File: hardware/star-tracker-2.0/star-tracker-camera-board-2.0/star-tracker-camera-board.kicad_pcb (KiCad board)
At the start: 4 copper layers, 31.5 x 13.6 mm, 43 parts, among them J1 3-1734742-6, U1 AR0134CSSM00SPCA0, U2 TPS70618DRVR, U3 TPS71928-28DRVT, U4 TPS71928-28DRVT, X1 MC2520Z27.0000C19XSH

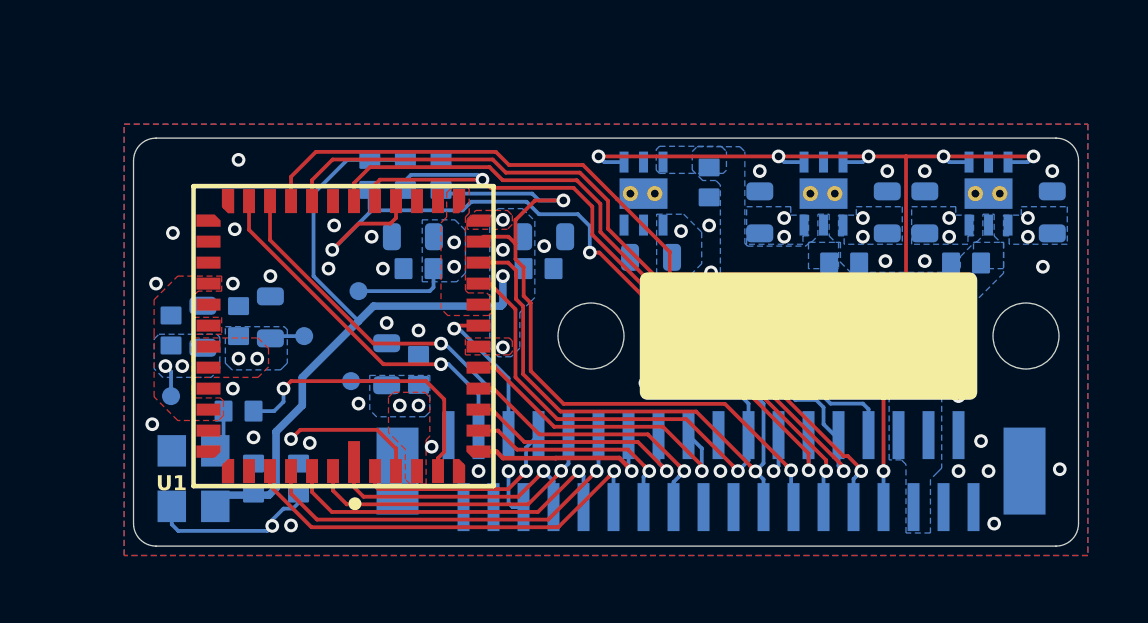
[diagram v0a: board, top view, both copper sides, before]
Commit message: Star tracker camera board
Fixing connector pin out so it fits on board well. Rotated sensor by 90 degrees. Started preliminary board layout
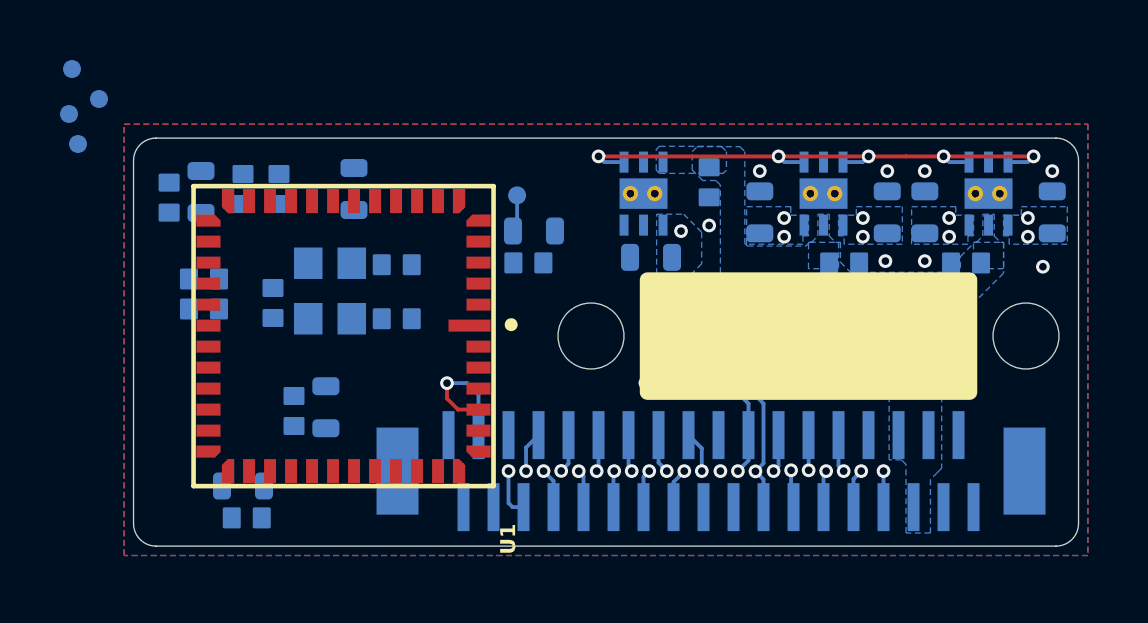
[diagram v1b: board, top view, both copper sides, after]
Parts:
- moved TP8 23.2 mm to (130.7, 95.9)
- moved TP6 11.3 mm to (130.6, 97.4)
- moved TP10 10.5 mm to (131.6, 96.9)
- moved C5 10.2 mm to (136.4, 99.9), turned to 90 degrees
- moved TP9 8.96 mm to (130.9, 98.4)
- moved C3 8.64 mm to (133.9, 100.2), turned to 90 degrees
- moved TP7 8.31 mm to (145.5, 100.1), turned to 90 degrees
- moved R11 8.07 mm to (135.1, 103.9), turned to 0 degrees
- moved X1 7.73 mm to (139.3, 103.3)
- moved C2 7.22 mm to (135.0, 100.0), turned to 90 degrees
- moved R2 7.18 mm to (141.5, 102.4)
- moved C1 7.15 mm to (141.5, 104.2), turned to 180 degrees
- moved C13 6.74 mm to (136.5, 110.9), turned to 180 degrees
- moved C8 6.62 mm to (146.1, 101.3), turned to 0 degrees
- moved C4 6.54 mm to (140.1, 99.9), turned to 90 degrees
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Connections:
- J1 pad 20: /D11 -> unconnected-(J1-Pad20)
- J1 pad 21: /D10 -> unconnected-(J1-Pad21)
- J1 pad 22: /D9 -> unconnected-(J1-Pad22)
- J1 pad 23: /D8 -> unconnected-(J1-Pad23)
- J1 pad 24: /D7 -> unconnected-(J1-Pad24)
- J1 pad 25: /D0 -> unconnected-(J1-Pad25)
- J1 pad 26: /D1 -> unconnected-(J1-Pad26)
- J1 pad 27: /D2 -> unconnected-(J1-Pad27)
- J1 pad 28: /D3 -> unconnected-(J1-Pad28)
- J1 pad 29: /D4 -> unconnected-(J1-Pad29)
- J1 pad 30: /D5 -> unconnected-(J1-Pad30)
- J1 pad 31: /D6 -> unconnected-(J1-Pad31)
- J1 pad 32: /PIXCLK -> unconnected-(J1-Pad32)
- J1 pad 33: /VSYNC -> unconnected-(J1-Pad33)
- J1 pad 34: /HSYNC -> /D0
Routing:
- net VDD_IO: track 40.4 -> 14.1 mm, vias 7 -> 2
- net /STANDBY: track 26.8 -> 1.17 mm, vias 3 -> 1
- net /SADDR: track 27.9 -> 2.41 mm
- net /TRIGGER: track 25.4 -> 0.00 mm, vias 1 -> 0
- net /FLASH: track 25.5 -> 1.36 mm
- net /~{OE}: track 24.7 -> 1.24 mm, vias 2 -> 1
- net /~{RESET}: track 24.0 -> 1.26 mm, vias 2 -> 1
- net /SDATA: track 20.5 -> 4.38 mm
- net /SCLK: track 18.4 -> 2.74 mm
- net /D6: track 14.8 -> 0.00 mm, vias 2 -> 0
- net /VSYNC: track 14.7 -> 0.00 mm, vias 1 -> 0
- net /VREG_EN: track 35.4 -> 22.1 mm, vias 7 -> 6
- net /D1: track 13.2 -> 0.00 mm, vias 1 -> 0
- net /HSYNC: track 12.2 -> 0.00 mm, vias 1 -> 0
- net /D2: track 11.7 -> 0.00 mm, vias 1 -> 0
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- removed copper zone on F.Cu, net VAA
- removed copper zone on F.Cu, net VAA_PIX
- removed copper zone on F.Cu, net VDD
- removed copper zone on F.Cu, net VDD_IO
- removed copper zone on F.Cu, net VDD_PLL

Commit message: Cleaned up files
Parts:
- moved TP8 23.2 mm to (152.6, 103.7)
- moved TP6 11.3 mm to (140.3, 103.3)
- moved TP10 10.5 mm to (138.4, 104.8)
- moved C5 10.2 mm to (146.3, 102.6), turned to 0 degrees
- moved TP9 8.96 mm to (134.0, 106.8)
- moved C3 8.64 mm to (142.3, 102.6), turned to 180 degrees
- moved TP7 8.31 mm to (140.0, 106.3), turned to 180 degrees
- moved R11 8.07 mm to (141.8, 99.4), turned to 90 degrees
- moved X1 7.73 mm to (134.8, 109.6)
- moved C2 7.22 mm to (142.1, 101.5), turned to 180 degrees
- moved R2 7.18 mm to (136.3, 107.3)
- moved C1 7.15 mm to (136.8, 109.6), turned to -90 degrees
- moved C13 6.74 mm to (134.0, 104.6), turned to 90 degrees
- moved C8 6.62 mm to (141.2, 105.7), turned to 90 degrees
- moved C4 6.54 mm to (146.4, 101.5), turned to 0 degrees
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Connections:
- J1 pad 20: unconnected-(J1-Pad20) -> /D11
- J1 pad 21: unconnected-(J1-Pad21) -> /D10
- J1 pad 22: unconnected-(J1-Pad22) -> /D9
- J1 pad 23: unconnected-(J1-Pad23) -> /D8
- J1 pad 24: unconnected-(J1-Pad24) -> /D7
- J1 pad 25: unconnected-(J1-Pad25) -> /D0
- J1 pad 26: unconnected-(J1-Pad26) -> /D1
- J1 pad 27: unconnected-(J1-Pad27) -> /D2
- J1 pad 28: unconnected-(J1-Pad28) -> /D3
- J1 pad 29: unconnected-(J1-Pad29) -> /D4
- J1 pad 30: unconnected-(J1-Pad30) -> /D5
- J1 pad 31: unconnected-(J1-Pad31) -> /D6
- J1 pad 32: unconnected-(J1-Pad32) -> /PIXCLK
- J1 pad 33: unconnected-(J1-Pad33) -> /VSYNC
- J1 pad 34: /D0 -> /HSYNC
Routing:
- net VDD_IO: track 14.1 -> 40.4 mm, vias 2 -> 7
- net /STANDBY: track 1.17 -> 26.8 mm, vias 1 -> 3
- net /SADDR: track 2.41 -> 27.9 mm
- net /TRIGGER: track 0.00 -> 25.4 mm, vias 0 -> 1
- net /FLASH: track 1.36 -> 25.5 mm
- net /~{OE}: track 1.24 -> 24.7 mm, vias 1 -> 2
- net /~{RESET}: track 1.26 -> 24.0 mm, vias 1 -> 2
- net /SDATA: track 4.38 -> 20.5 mm
- net /SCLK: track 2.74 -> 18.4 mm
- net /D6: track 0.00 -> 14.8 mm, vias 0 -> 2
- net /VSYNC: track 0.00 -> 14.7 mm, vias 0 -> 1
- net /VREG_EN: track 22.1 -> 35.4 mm, vias 6 -> 7
- net /D1: track 0.00 -> 13.2 mm, vias 0 -> 1
- net /HSYNC: track 0.00 -> 12.2 mm, vias 0 -> 1
- net /D2: track 0.00 -> 11.7 mm, vias 0 -> 1
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- added copper zone on F.Cu, net VAA
- added copper zone on F.Cu, net VAA_PIX
- added copper zone on F.Cu, net VDD
- added copper zone on F.Cu, net VDD_IO
- added copper zone on F.Cu, net VDD_PLL

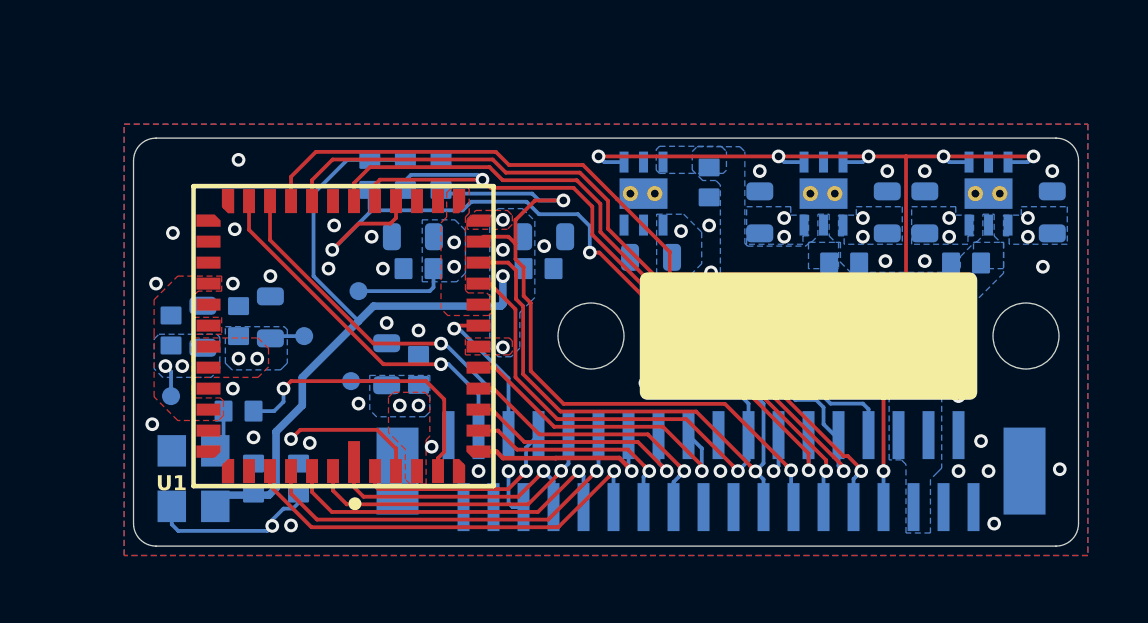
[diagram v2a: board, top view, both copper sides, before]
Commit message: Update
Layout complete, 90% finished routing.
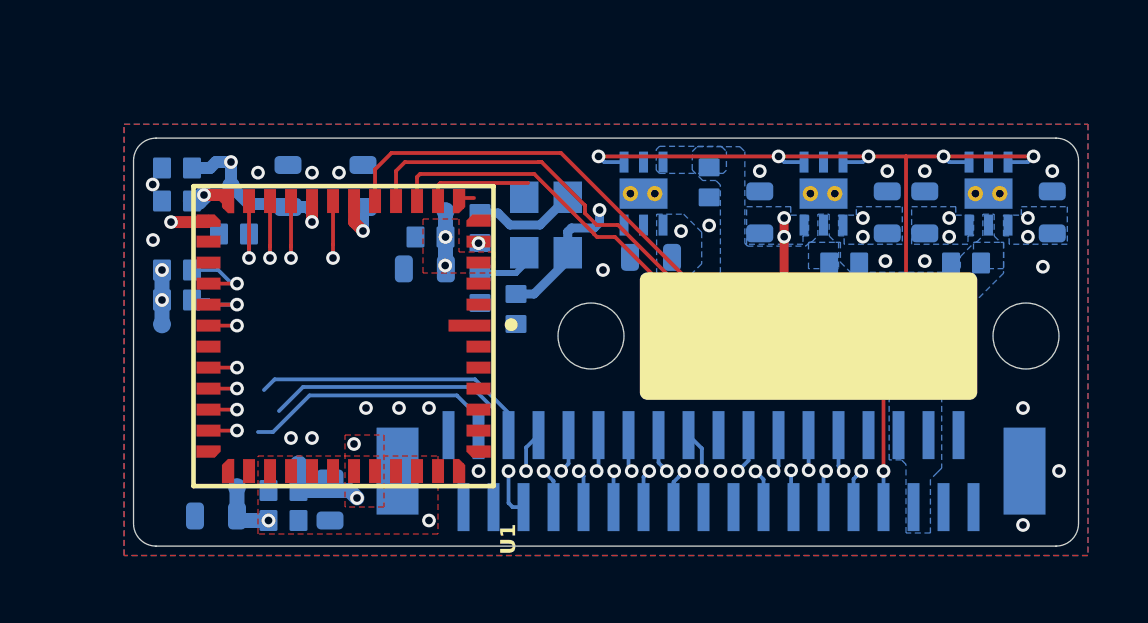
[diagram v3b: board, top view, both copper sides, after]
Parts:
- moved TP8 18.9 mm to (133.7, 104.4)
- moved X1 14.5 mm to (146.5, 101.1)
- moved C5 12.3 mm to (134.2, 100.3), turned to 180 degrees
- moved C1 10.4 mm to (145.5, 103.9), turned to 90 degrees
- moved R2 10.1 mm to (144.3, 101.2), turned to -90 degrees
- moved R12 8.77 mm to (144.3, 103.2), turned to 90 degrees
- moved C3 8.72 mm to (134.2, 99.2)
- moved R11 8.68 mm to (134.2, 103.6), turned to 180 degrees
- moved C13 7.36 mm to (137.8, 111.0), turned to 0 degrees
- moved R9 7.18 mm to (136.1, 101.4), turned to 0 degrees
- moved R10 7.17 mm to (134.2, 102.6), turned to 180 degrees
- moved TP7 6.48 mm to (143.2, 100.6), turned to -90 degrees
- moved C16 6.39 mm to (139.3, 110.2), turned to -90 degrees
- moved C12 6.32 mm to (135.5, 110.8), turned to 180 degrees
- moved C4 6.27 mm to (140.4, 99.8), turned to 90 degrees
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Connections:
- J1 pad 10: /SADDR -> unconnected-(J1-Pad10)
- J1 pad 11: /~{OE} -> unconnected-(J1-Pad11)
- J1 pad 12: /STANDBY -> unconnected-(J1-Pad12)
- J1 pad 13: /~{RESET} -> unconnected-(J1-Pad13)
- J1 pad 14: /CLK_EN -> unconnected-(J1-Pad14)
- J1 pad 15: /SDATA -> unconnected-(J1-Pad15)
- J1 pad 16: /SCLK -> unconnected-(J1-Pad16)
- J1 pad 20: /D11 -> unconnected-(J1-Pad20)
- J1 pad 21: /D10 -> unconnected-(J1-Pad21)
- J1 pad 22: /D9 -> unconnected-(J1-Pad22)
- J1 pad 23: /D8 -> unconnected-(J1-Pad23)
- J1 pad 24: /D7 -> unconnected-(J1-Pad24)
- J1 pad 25: /D0 -> unconnected-(J1-Pad25)
- J1 pad 26: /D1 -> unconnected-(J1-Pad26)
- J1 pad 27: /D2 -> unconnected-(J1-Pad27)
- J1 pad 28: /D3 -> unconnected-(J1-Pad28)
- J1 pad 29: /D4 -> unconnected-(J1-Pad29)
- J1 pad 30: /D5 -> unconnected-(J1-Pad30)
- J1 pad 31: /D6 -> unconnected-(J1-Pad31)
- J1 pad 32: /PIXCLK -> unconnected-(J1-Pad32)
- J1 pad 33: /VSYNC -> unconnected-(J1-Pad33)
- J1 pad 34: /HSYNC -> unconnected-(J1-Pad34)
- J1 pad 8: /TRIGGER -> unconnected-(J1-Pad8)
- J1 pad 9: /FLASH -> unconnected-(J1-Pad9)
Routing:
- net /SADDR: track 27.9 -> 1.95 mm
- net /FLASH: track 25.5 -> 0.95 mm
- net /TRIGGER: track 25.4 -> 0.95 mm
- net /STANDBY: track 26.8 -> 2.64 mm, vias 3 -> 1
- net /CLK_EN: track 24.6 -> 1.99 mm, vias 2 -> 0
- net /~{OE}: track 24.7 -> 2.51 mm, vias 2 -> 1
- net /~{RESET}: track 24.0 -> 2.70 mm, vias 2 -> 1
- net /SDATA: track 20.5 -> 1.90 mm
- net /SCLK: track 18.4 -> 1.90 mm
- net VDD: track 12.9 -> 27.8 mm, vias 3 -> 4
- net /D6: track 14.8 -> 0.00 mm, vias 2 -> 0
- net /D0: track 14.5 -> 0.00 mm, vias 1 -> 0
- net /VSYNC: track 14.7 -> 0.95 mm
- net /D1: track 13.2 -> 0.00 mm, vias 1 -> 0
- net /D2: track 11.7 -> 0.00 mm, vias 1 -> 0
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- removed copper zone on F.Cu, net VDD
- removed copper zone on F.Cu, net VDD_IO

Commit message: Update on camera board
Finished layout and routing. Only needs DRC error fixing and silk screen placement
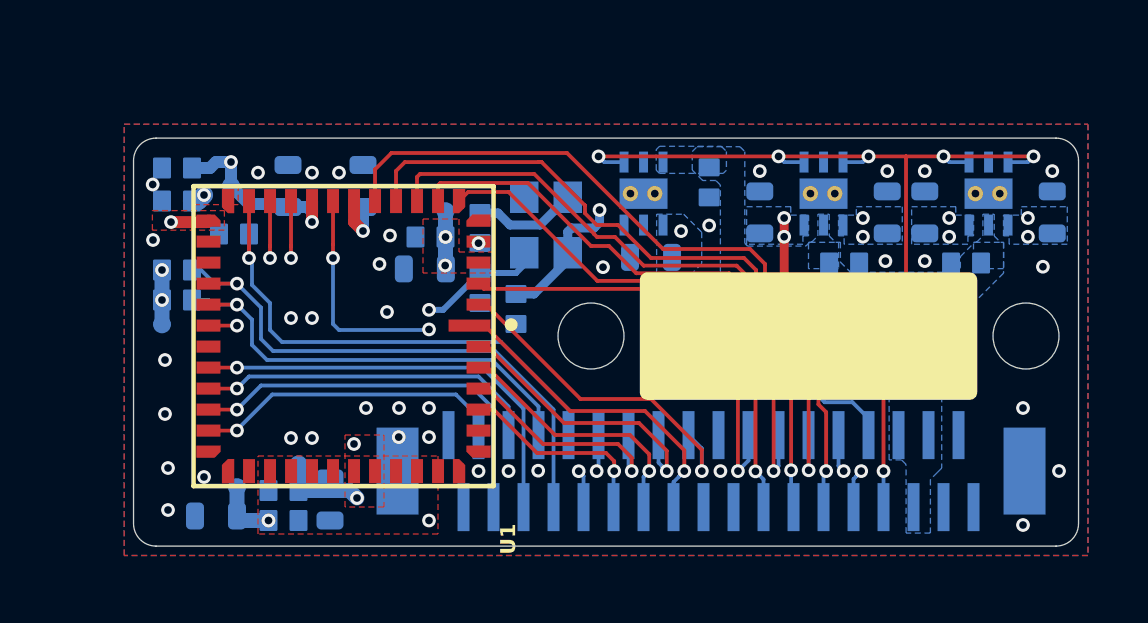
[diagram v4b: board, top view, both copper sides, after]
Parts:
- moved R7 1.03 mm to (153.0, 105.3)
- moved R8 1.00 mm to (151.9, 105.3)
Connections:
- J1 pad 10: unconnected-(J1-Pad10) -> /SDATA
- J1 pad 11: unconnected-(J1-Pad11) -> /D11
- J1 pad 12: unconnected-(J1-Pad12) -> /D10
- J1 pad 13: unconnected-(J1-Pad13) -> /D9
- J1 pad 14: unconnected-(J1-Pad14) -> /D8
- J1 pad 15: unconnected-(J1-Pad15) -> /D7
- J1 pad 16: unconnected-(J1-Pad16) -> /D6
- J1 pad 20: unconnected-(J1-Pad20) -> /D5
- J1 pad 21: unconnected-(J1-Pad21) -> /D4
- J1 pad 22: unconnected-(J1-Pad22) -> /D3
- J1 pad 23: unconnected-(J1-Pad23) -> /D2
- J1 pad 24: unconnected-(J1-Pad24) -> /D1
- J1 pad 25: unconnected-(J1-Pad25) -> /D0
- J1 pad 26: unconnected-(J1-Pad26) -> /CLK_EN
- J1 pad 27: unconnected-(J1-Pad27) -> /PIXCLK
- J1 pad 28: unconnected-(J1-Pad28) -> /~{RESET}
- J1 pad 29: unconnected-(J1-Pad29) -> /STANDBY
- J1 pad 30: unconnected-(J1-Pad30) -> /~{OE}
- J1 pad 31: unconnected-(J1-Pad31) -> /FLASH
- J1 pad 32: unconnected-(J1-Pad32) -> /TRIGGER
- J1 pad 33: unconnected-(J1-Pad33) -> /VSYNC
- J1 pad 34: unconnected-(J1-Pad34) -> /HSYNC
- J1 pad 8: unconnected-(J1-Pad8) -> /SADDR
- J1 pad 9: unconnected-(J1-Pad9) -> /SCLK
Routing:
- net /SDATA: track 1.90 -> 27.9 mm, vias 1 -> 3
- net /SCLK: track 1.90 -> 27.8 mm, vias 1 -> 3
- net /SADDR: track 1.95 -> 26.6 mm, vias 1 -> 2
- net /D7: track 0.54 -> 18.2 mm, vias 0 -> 1
- net /D8: track 3.56 -> 20.0 mm, vias 0 -> 1
- net /STANDBY: track 2.64 -> 18.8 mm
- net /D6: track 0.00 -> 15.7 mm, vias 0 -> 1
- net /PIXCLK: track 1.90 -> 17.0 mm, vias 1 -> 3
- net /~{RESET}: track 2.70 -> 17.3 mm
- net /FLASH: track 0.95 -> 14.3 mm
- net /~{OE}: track 2.51 -> 15.4 mm
- net /CLK_EN: track 1.99 -> 14.7 mm, vias 0 -> 2
- net /VSYNC: track 0.95 -> 13.4 mm
- net /D5: track 0.00 -> 11.5 mm, vias 0 -> 1
- net unconnected-(J1-Pad33): track 11.1 -> 0.00 mm
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- added copper zone on F.Cu, net VDD
- added copper zone on F.Cu, net VDD_IO

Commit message: Finished Camera Board ready for DR
fixed all silkscreen warnings and DRC errors. Ready for DR.
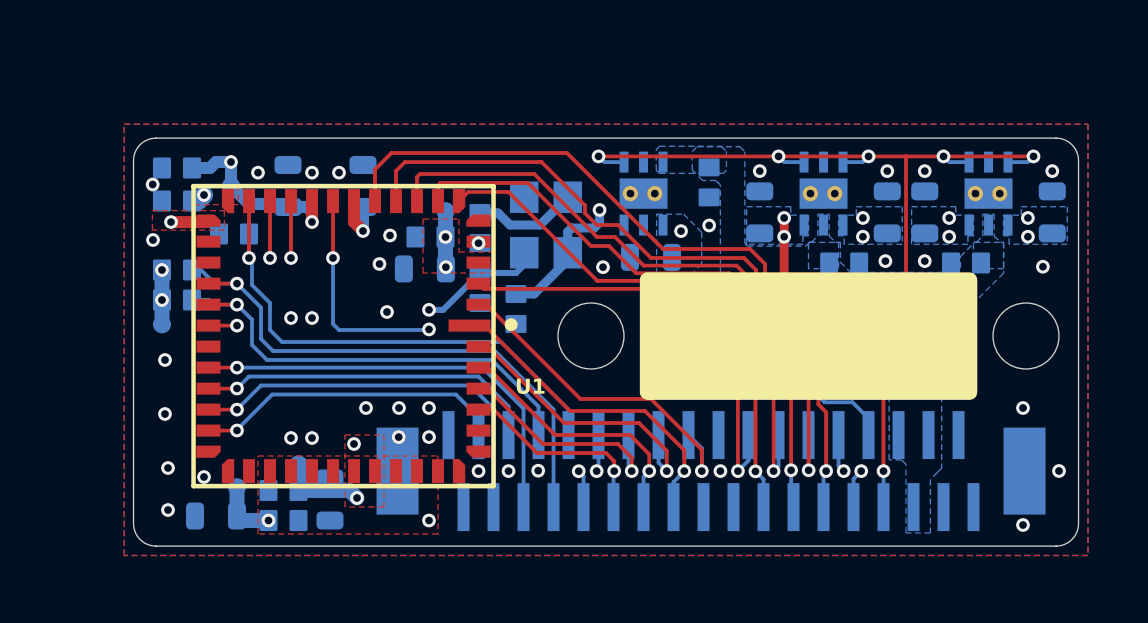
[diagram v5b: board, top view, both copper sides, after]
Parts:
- moved R7 0.15 mm to (152.8, 105.3)
- moved R8 0.15 mm to (151.8, 105.3)
- moved R5 0.10 mm to (157.1, 105.3)
- moved R6 0.10 mm to (156.1, 105.3)
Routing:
- net VAA: track 36.0 -> 35.4 mm

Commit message: Routine Push
Updated schematic and layout. about 60% done with routing.
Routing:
- net Net-(X1-OUT): track 3.47 -> 5.12 mm
- net /PIXCLK: track 17.0 -> 16.2 mm
- net VDD_PLL: track 17.8 -> 18.5 mm
- net /D7: track 18.2 -> 17.5 mm
- net /CLK_EN: track 14.7 -> 14.0 mm
- net GND: vias 43 -> 45

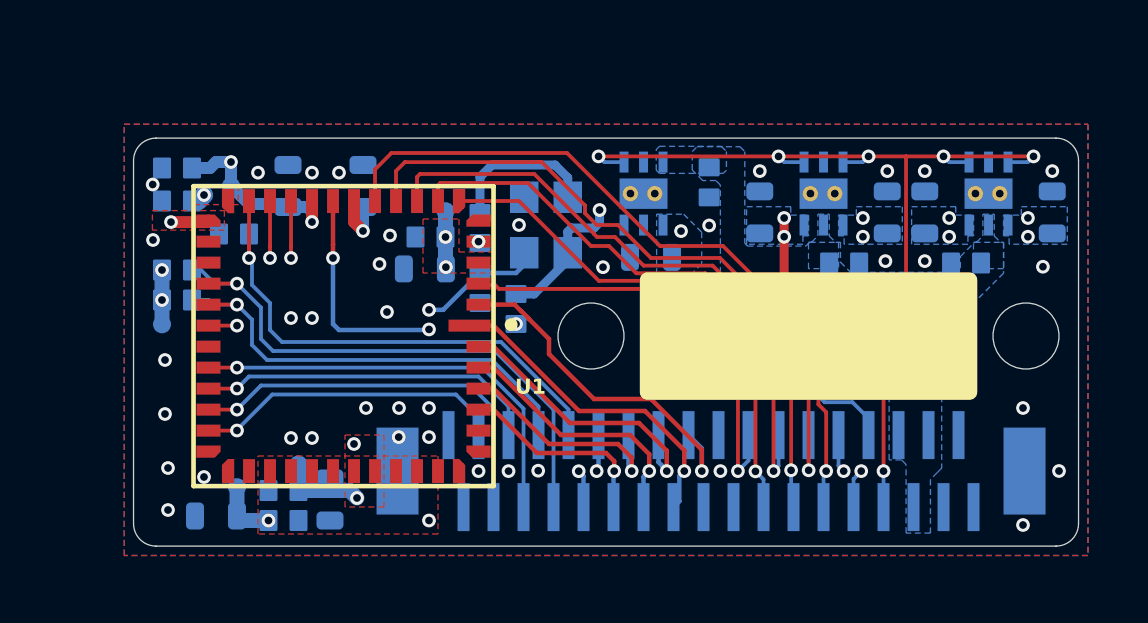
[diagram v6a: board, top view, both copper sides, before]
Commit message: Star tracker board update
Added 3d models to footprints, reannotated component designators
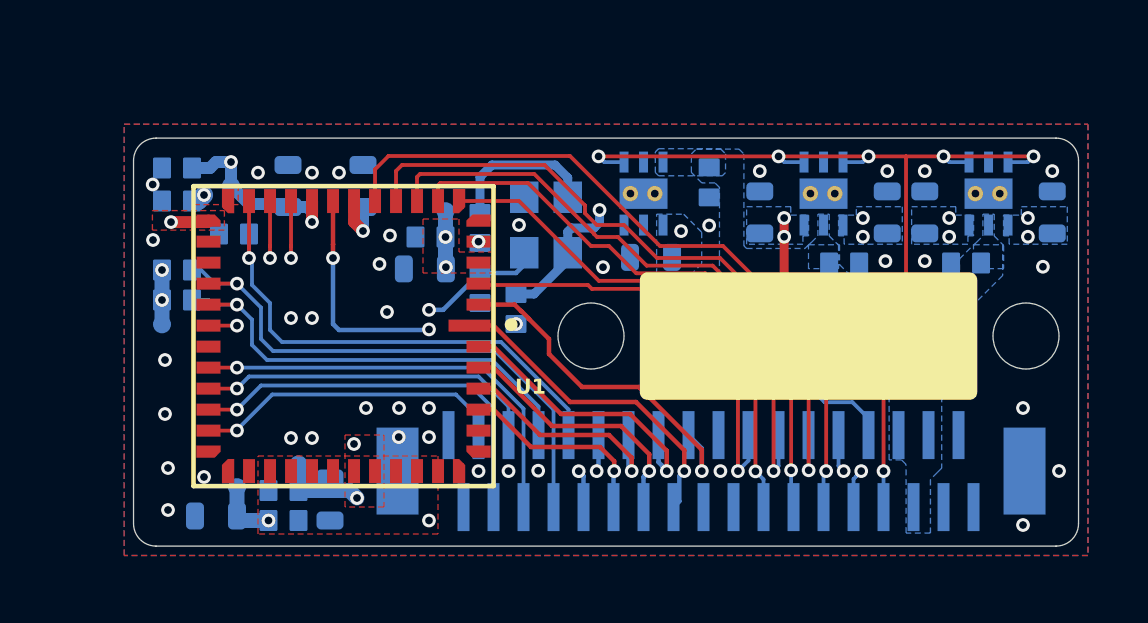
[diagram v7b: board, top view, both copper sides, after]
